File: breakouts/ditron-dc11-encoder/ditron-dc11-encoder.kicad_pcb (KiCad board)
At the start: 2 copper layers, 30 x 37 mm, 5 parts, among them J1 DB9_Receptacle, J2 RJ45_LED_Shielded

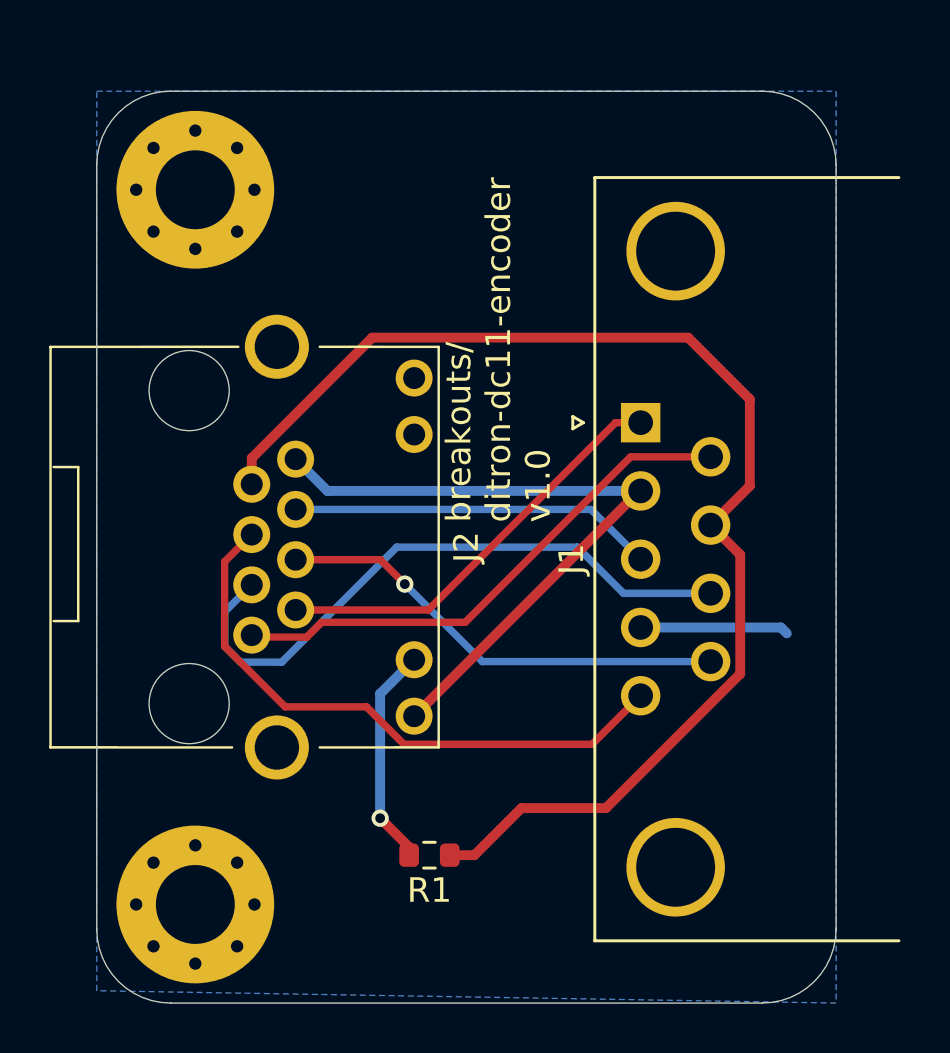
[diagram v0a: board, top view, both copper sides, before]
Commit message: Update breakouts/ditron-dc11-encoder: enlarge the PCB slightly
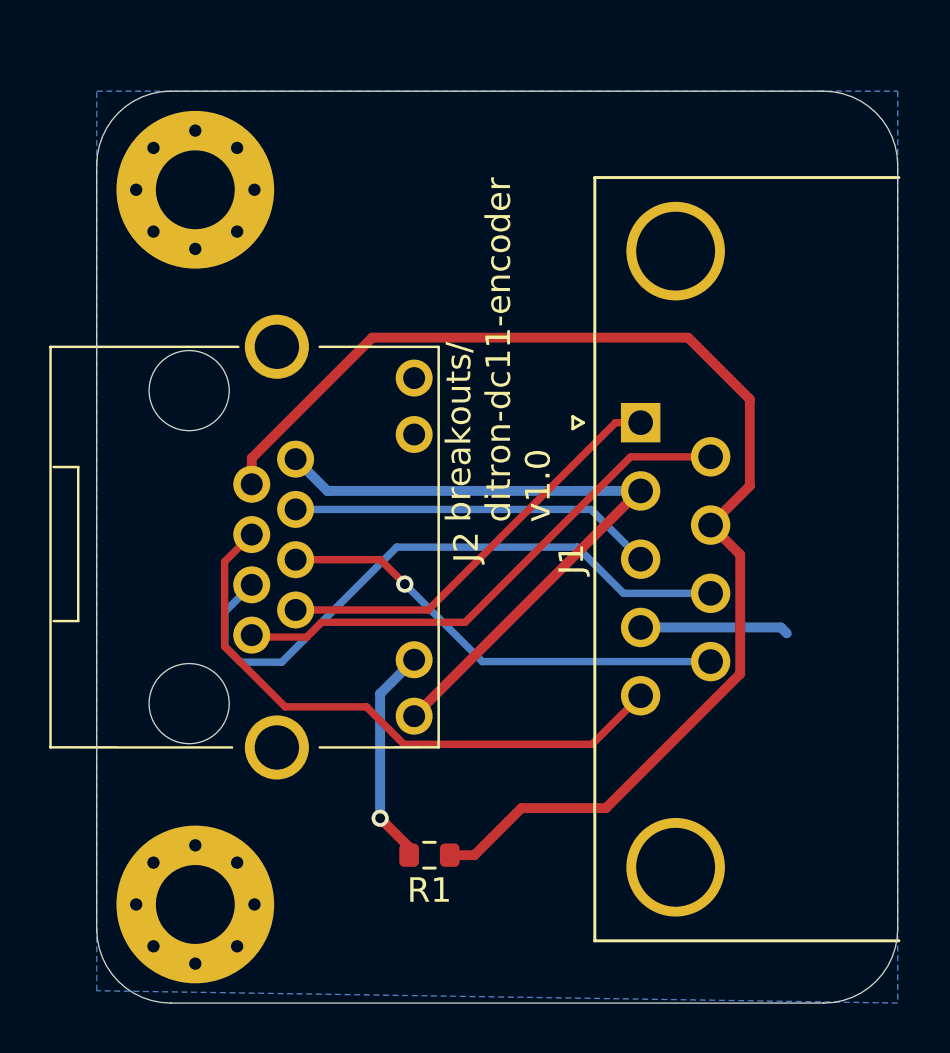
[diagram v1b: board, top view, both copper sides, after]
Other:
- board size 30 x 37 mm -> 32.5 x 37 mm
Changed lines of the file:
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@@
 		(tags "resistor")
 		(property "Reference" "R1"
-			(at 0 -1.43 360)
+			(at 0 -1.43 0)
 			(layer "F.SilkS")
 			(effects
@@
 		)
 		(property "Value" "3K3"
-			(at 0 1.43 360)
+			(at 0 1.43 0)
 			(layer "F.Fab")
 			(effects
@@
 		)
 		(fp_text user "${REFERENCE}"
-			(at -0.675 0 360)
+			(at -0.675 0 0)
 			(layer "F.Fab")
 			(effects
@@
 	(gr_line
 		(start 150 75)
-		(end 174 75)
+		(end 176.5 75)
 		(stroke
 			(width 0.05)
@@
 	)
 	(gr_arc
-		(start 174 75)
-		(mid 176.12132 75.87868)
-		(end 177 78)
+		(start 176.5 75)
+		(mid 178.62132 75.87868)
+		(end 179.5 78)
 		(stroke
 			(width 0.05)
@@
 	)
 	(gr_arc
-		(start 177 109)
-		(mid 176.12132 111.12132)
-		(end 174 112)
+		(start 179.5 109)
+		(mid 178.62132 111.12132)
+		(end 176.5 112)
 		(stroke
 			(width 0.05)
@@
 	)
 	(gr_line
-		(start 177 78)
-		(end 177 109)
+		(start 179.5 78)
+		(end 179.5 109)
 		(stroke
 			(width 0.05)
@@
 	)
 	(gr_line
-		(start 174 112)
+		(start 176.5 112)
 		(end 150 112)
 		(stroke
@@
 		(polygon
 			(pts
-				(xy 147 75) (xy 177 75) (xy 177 112) (xy 147 111.5)
-			)
-		)
+				(xy 147 75) (xy 179.5 75) (xy 179.5 112) (xy 147 111.5)
+			)
+		)
